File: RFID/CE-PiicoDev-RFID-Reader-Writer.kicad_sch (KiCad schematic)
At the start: 32 parts, among them U1 MFRC522, Y1 27.12MHz 12pF

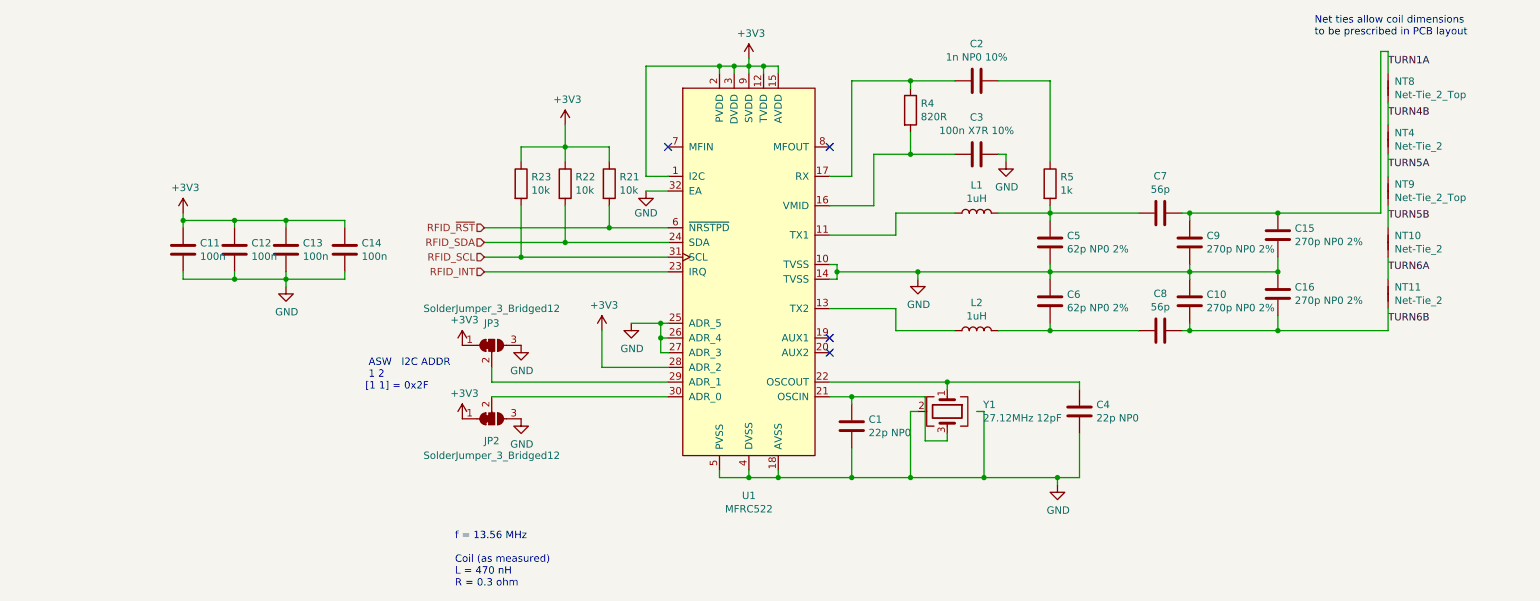
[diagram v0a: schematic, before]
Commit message: Renamed duplicate references.
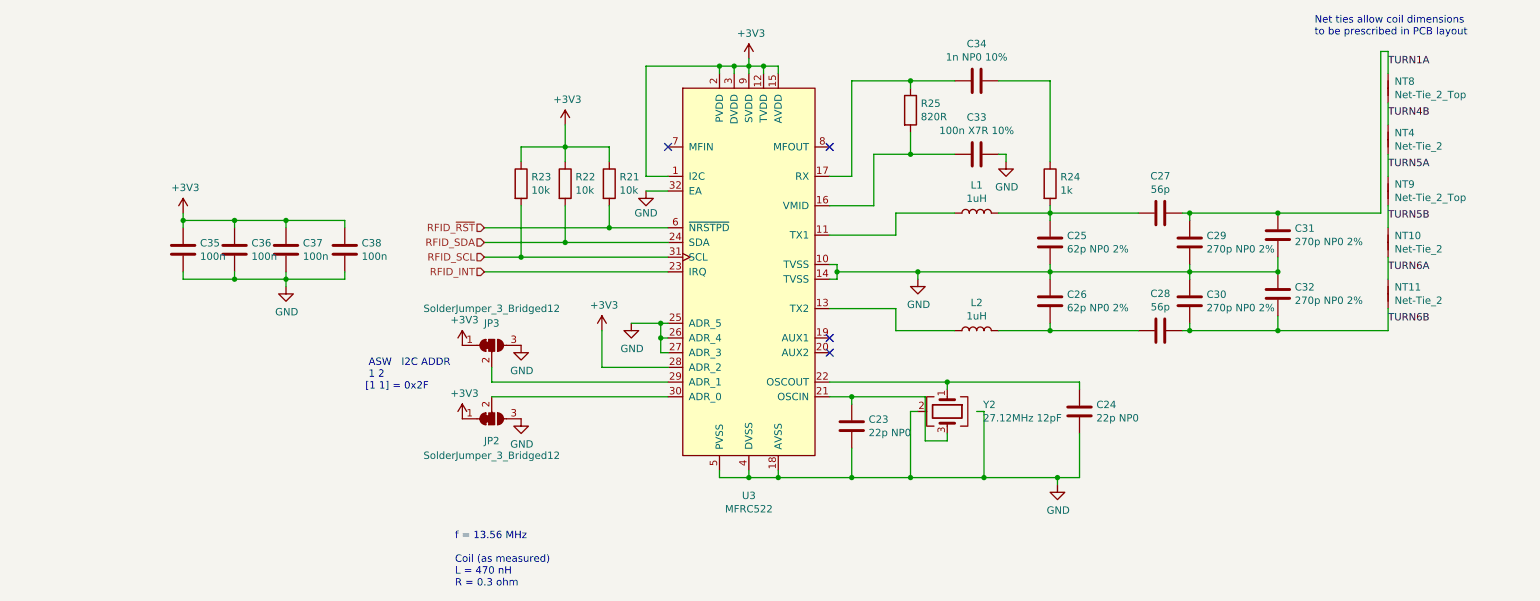
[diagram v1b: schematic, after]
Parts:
- removed C4: 22p NP0, Capacitor_SMD:C_0402_1005Metric, symbol Device:C
- added C24: 22p NP0, Capacitor_SMD:C_0402_1005Metric, symbol Device:C
- renumbered C1 to C23, C5 to C25, C6 to C26, C7 to C27, C8 to C28, C9 to C29, C10 to C30, C15 to C31, C16 to C32, C3 to C33, C2 to C34, C11 to C35, C12 to C36, C13 to C37, C14 to C38, R5 to R24, R4 to R25, U1 to U3, Y1 to Y2
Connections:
- net GND: now also C24.2
- net at U3.22 (OSCOUT), Y2.1: now also C24.1

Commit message: Attached part number to components.
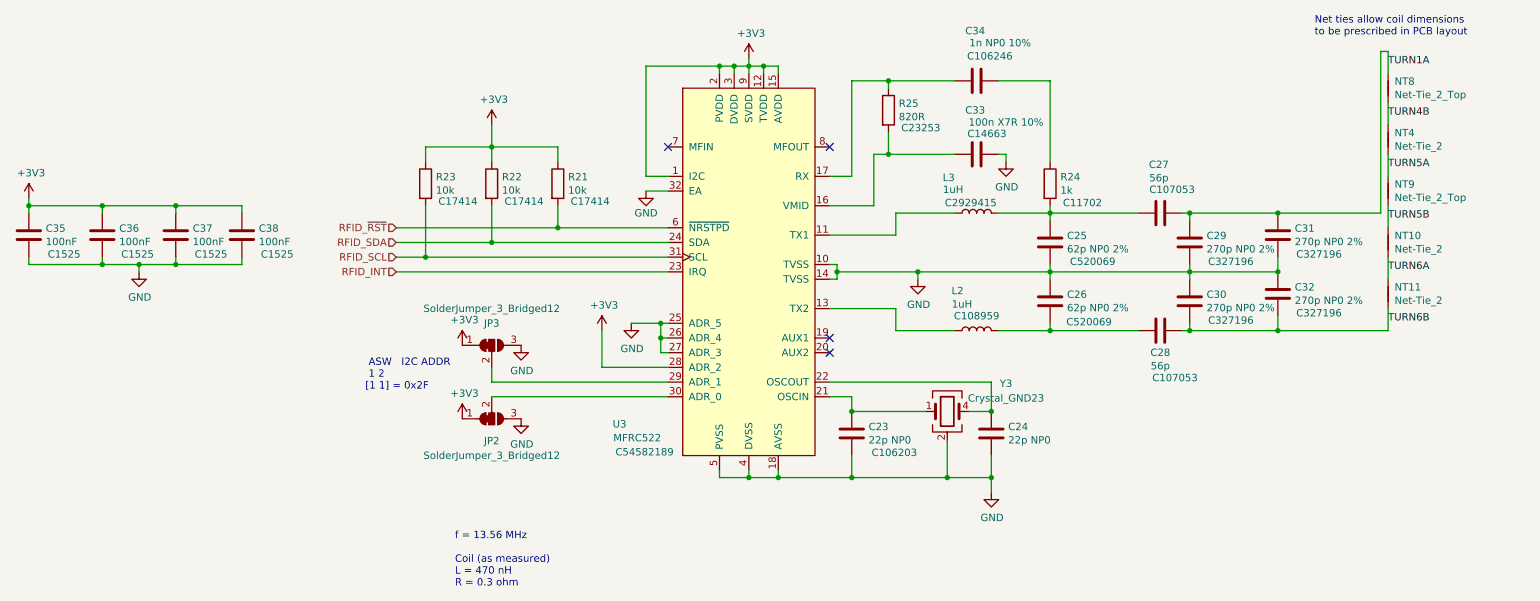
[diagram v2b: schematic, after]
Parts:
- removed Y2: 27.12MHz 12pF, Crystal:Crystal_SMD_TXC_7M-4Pin_3.2x2.5mm, symbol Device:Crystal_GND24
- added Y3: Crystal_GND23, symbol Device:Crystal_GND23
- C23, C24: LCSC PN (none) -> C106203
- C25, C26: footprint Capacitor_SMD:C_0603_1608Metric -> Capacitor_SMD:C_0805_2012Metric; LCSC PN (none) -> C520069
- C27, C28: LCSC PN (none) -> C107053
- C29, C30, C31, C32: LCSC PN (none) -> C327196
- C33: footprint Capacitor_SMD:C_0402_1005Metric -> Capacitor_SMD:C_0603_1608Metric; LCSC PN (none) -> C14663
- C34: LCSC PN (none) -> C106246
- C35, C36, C37, C38: value 100n -> 100nF; LCSC PN (none) -> C1525
- L2: LCSC PN (none) -> C108959
- L3: renamed from L1; footprint Inductor_SMD:L_0603_1608Metric -> SamacSys_Parts:IND-SMD_L4.5-W4.0; LCSC PN (none) -> C2929415
- R21, R22, R23: footprint Resistor_SMD:R_0402_1005Metric -> Resistor_SMD:R_0805_2012Metric; LCSC PN (none) -> C17414
- R24: footprint Resistor_SMD:R_0603_1608Metric -> Resistor_SMD:R_0402_1005Metric; LCSC PN (none) -> C11702
- R25: LCSC PN (none) -> C23253
- U3: LCSC PN (none) -> C54582189
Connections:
- net GND: now also Y3.2 (G), Y3.3 (G)
- net at C24.1, U3.22 (OSCOUT): now also Y3.4
- net at C23.1, U3.21 (OSCIN): now also Y3.1
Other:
- moved on the sheet: C23, C24, C35, C36, C37, C38, R21, R22, R23, R25

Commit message: Add footprint to xtal oscillator.
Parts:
- Y3: footprint (none) -> Crystal:Crystal_SMD_3225-4Pin_3.2x2.5mm
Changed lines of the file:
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@@
 			)
 		)
-		(property "Footprint" ""
+		(property "Footprint" "Crystal:Crystal_SMD_3225-4Pin_3.2x2.5mm"
 			(at 187.96 104.14 0)
 			(hide yes)

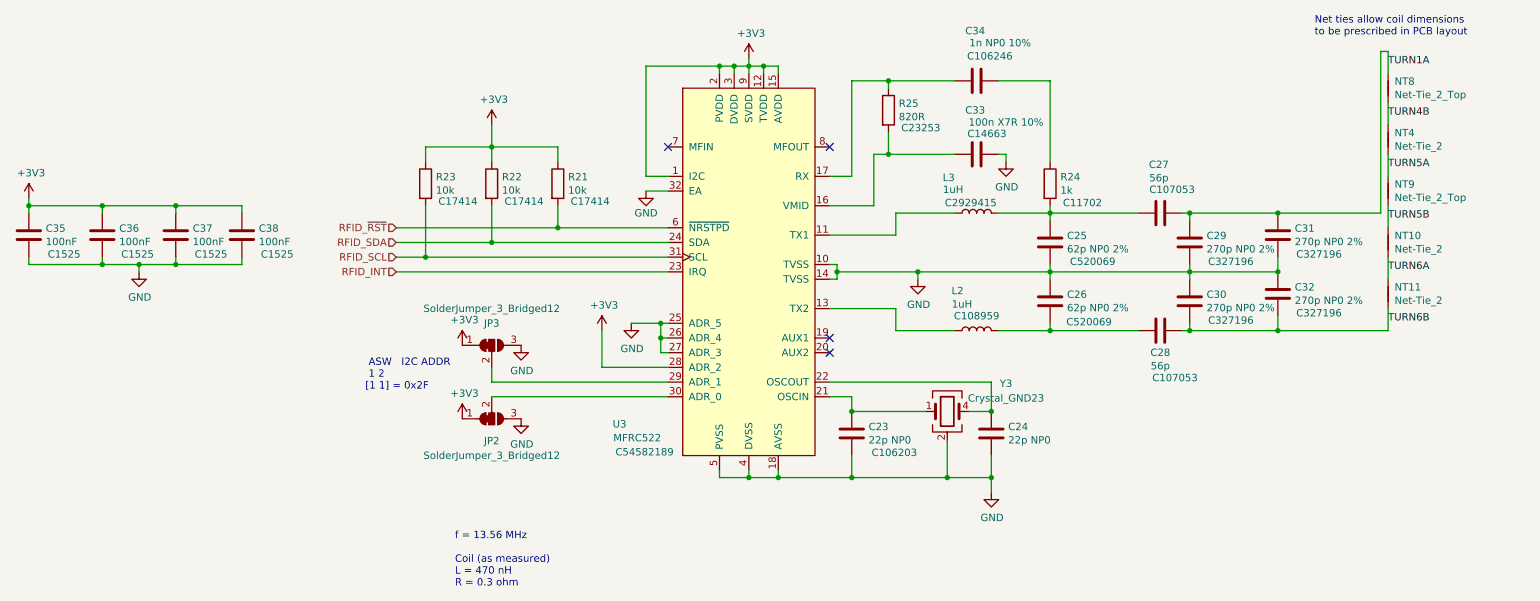
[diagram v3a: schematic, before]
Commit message: Fix ERC errors.
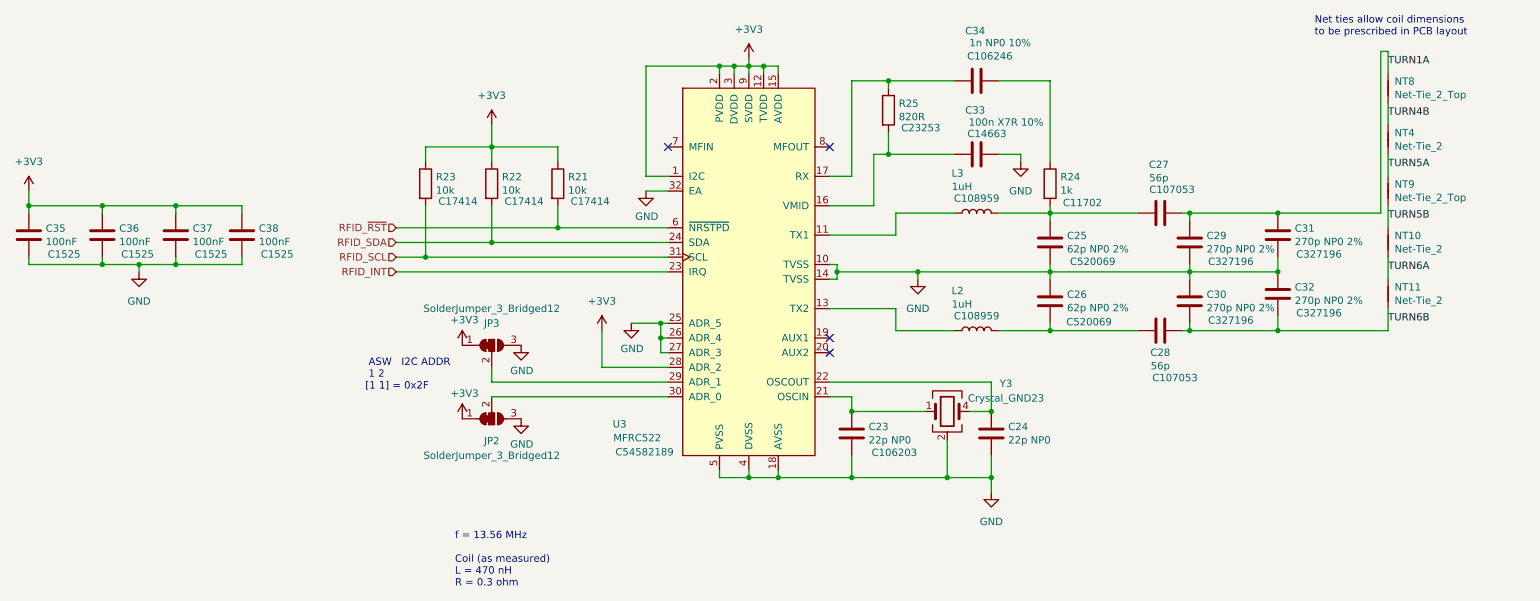
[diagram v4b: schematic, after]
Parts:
- L3: footprint SamacSys_Parts:IND-SMD_L4.5-W4.0 -> Inductor_SMD:L_0603_1608Metric; LCSC PN C2929415 -> C108959

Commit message: Fix ERC errors.
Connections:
- net RFID_INT renamed RFID_IQR
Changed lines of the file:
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@@
 		)
 	)
-	(hierarchical_label "RFID_INT"
+	(hierarchical_label "RFID_IQR"
 		(shape input)
 		(at 92.71 80.01 180)

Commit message: Add part numbers for USB C and RFID xtal.
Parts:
- removed Y3: Crystal_GND23, Crystal:Crystal_SMD_3225-4Pin_3.2x2.5mm, symbol Device:Crystal_GND23
- added Y2: Crystal_GND23, Crystal:Crystal_SMD_3225-4Pin_3.2x2.5mm, symbol Device:Crystal_GND23
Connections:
- net GND: now also Y2.2 (G), Y2.3 (G)
- net at C23.1, U3.21 (OSCIN): now also Y2.1
- net at C24.1, U3.22 (OSCOUT): now also Y2.4
